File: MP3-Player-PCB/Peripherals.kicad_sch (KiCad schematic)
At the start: 8 parts, among them J401 Micro_SD_Card, Q401 AO3401A, SW401 1-1825910-4, SW402 1-1825910-4, SW403 1-1825910-4, SW404 1-1825910-4

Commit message: Started power schematic
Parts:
- renumbered D401 to D301, D402 to D302, J401 to J301, Q401 to Q301, SW401 to SW301, SW402 to SW302, SW403 to SW303, SW404 to SW304
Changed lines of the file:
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@@
 		(dnp no)
 		(fields_autoplaced yes)
-		(property "Reference" "D402"
+		(property "Reference" "D302"
 			(at 189.23 82.4798 0)
 			(effects
@@
 			(project "MP3-Player"
 				(path "/3f51ea9b-d2e1-4711-a47c-269e1b97e0f4/425fb02a-335c-42f3-aa7e-942bbee7b5dd"
-					(reference "D402")
+					(reference "D302")
 					(unit 1)
 				)
@@
 		(dnp no)
 		(fields_autoplaced yes)
-		(property "Reference" "SW402"
+		(property "Reference" "SW302"
 			(at 93.98 40.64 0)
 			(effects
@@
 			(project "MP3-Player"
 				(path "/3f51ea9b-d2e1-4711-a47c-269e1b97e0f4/425fb02a-335c-42f3-aa7e-942bbee7b5dd"
-					(reference "SW402")
+					(reference "SW302")
 					(unit 1)
 				)
@@
 		(dnp no)
 		(fields_autoplaced yes)
-		(property "Reference" "SW403"
+		(property "Reference" "SW303"
 			(at 72.39 54.61 0)
 			(effects
@@
 			(project "MP3-Player"
 				(path "/3f51ea9b-d2e1-4711-a47c-269e1b97e0f4/425fb02a-335c-42f3-aa7e-942bbee7b5dd"
-					(reference "SW403")
+					(reference "SW303")
 					(unit 1)
 				)
@@
 		(dnp no)
 		(fields_autoplaced yes)
-		(property "Reference" "SW404"
+		(property "Reference" "SW304"
 			(at 93.98 54.61 0)
 			(effects
@@
 			(project "MP3-Player"
 				(path "/3f51ea9b-d2e1-4711-a47c-269e1b97e0f4/425fb02a-335c-42f3-aa7e-942bbee7b5dd"
-					(reference "SW404")
+					(reference "SW304")
 					(unit 1)
 				)
@@
 		(dnp no)
 		(fields_autoplaced yes)
-		(property "Reference" "Q401"
+		(property "Reference" "Q301"
 			(at 121.92 87.6299 0)
 			(effects
@@
 			(project ""
 				(path "/3f51ea9b-d2e1-4711-a47c-269e1b97e0f4/425fb02a-335c-42f3-aa7e-942bbee7b5dd"
-					(reference "Q401")
+					(reference "Q301")
 					(unit 1)
 				)
@@
 		(dnp no)
 		(fields_autoplaced yes)
-		(property "Reference" "D401"
+		(property "Reference" "D301"
 			(at 156.21 82.4798 0)
 			(effects
@@
 			(project "MP3-Player"
 				(path "/3f51ea9b-d2e1-4711-a47c-269e1b97e0f4/425fb02a-335c-42f3-aa7e-942bbee7b5dd"
-					(reference "D401")
+					(reference "D301")
 					(unit 1)
 				)
@@
 		(dnp no)
 		(fields_autoplaced yes)
-		(property "Reference" "SW401"
+		(property "Reference" "SW301"
 			(at 72.39 40.64 0)
 			(effects
@@
 			(project ""
 				(path "/3f51ea9b-d2e1-4711-a47c-269e1b97e0f4/425fb02a-335c-42f3-aa7e-942bbee7b5dd"
-					(reference "SW401")
+					(reference "SW301")
 					(unit 1)
 				)
@@
 		(dnp no)
 		(fields_autoplaced yes)
-		(property "Reference" "J401"
+		(property "Reference" "J301"
 			(at 156.845 34.29 0)
 			(effects
@@
 			(project "MP3-Player"
 				(path "/3f51ea9b-d2e1-4711-a47c-269e1b97e0f4/425fb02a-335c-42f3-aa7e-942bbee7b5dd"
-					(reference "J401")
-					(unit 1)
-				)
+					(reference "J301")
+					(unit 1)
+				)

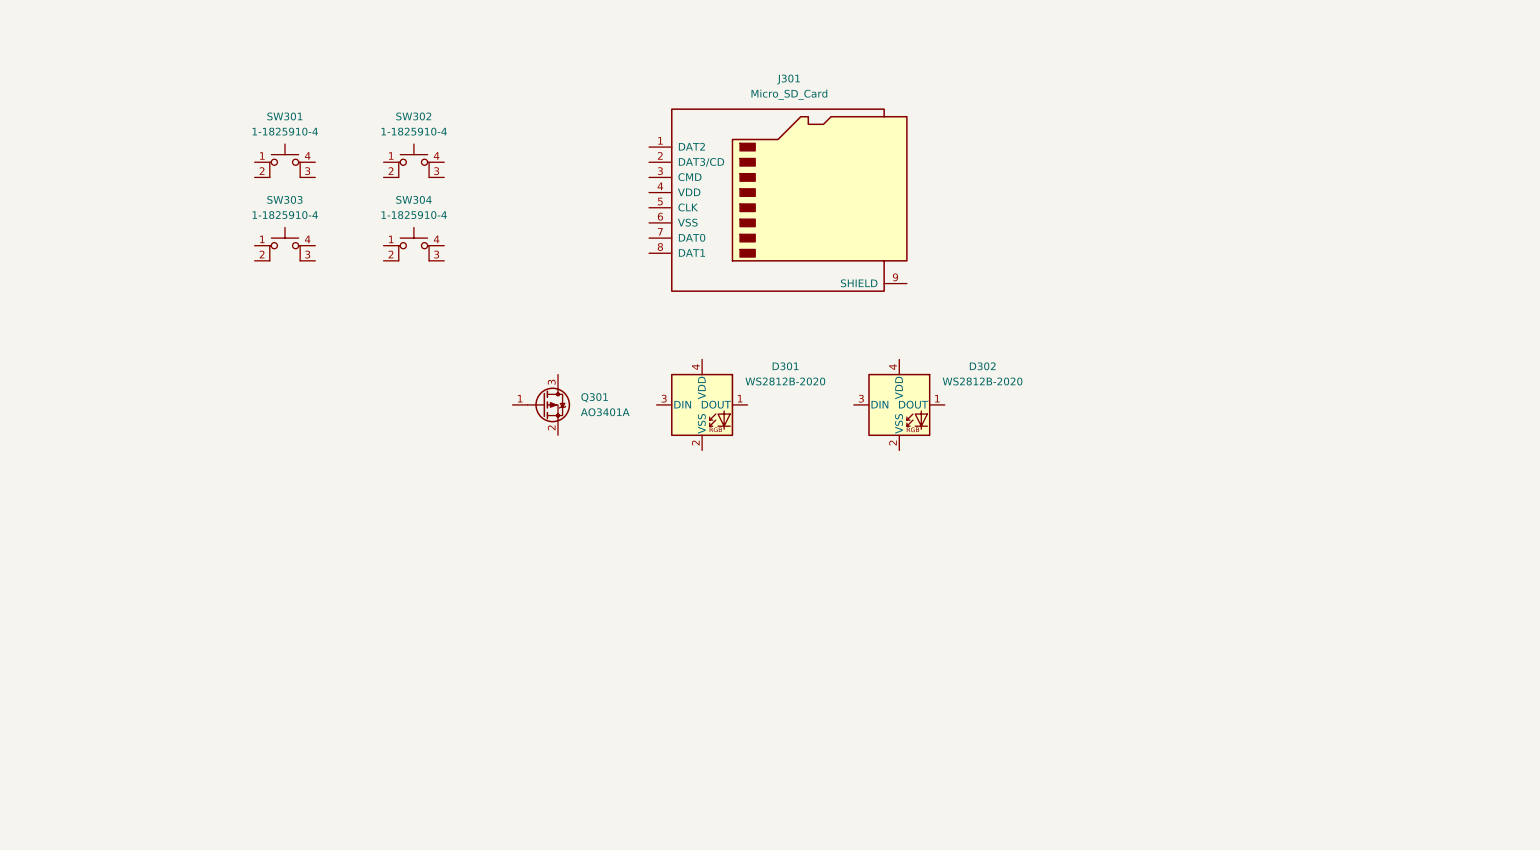
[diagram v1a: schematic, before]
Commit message: Added addressable LED circuitry
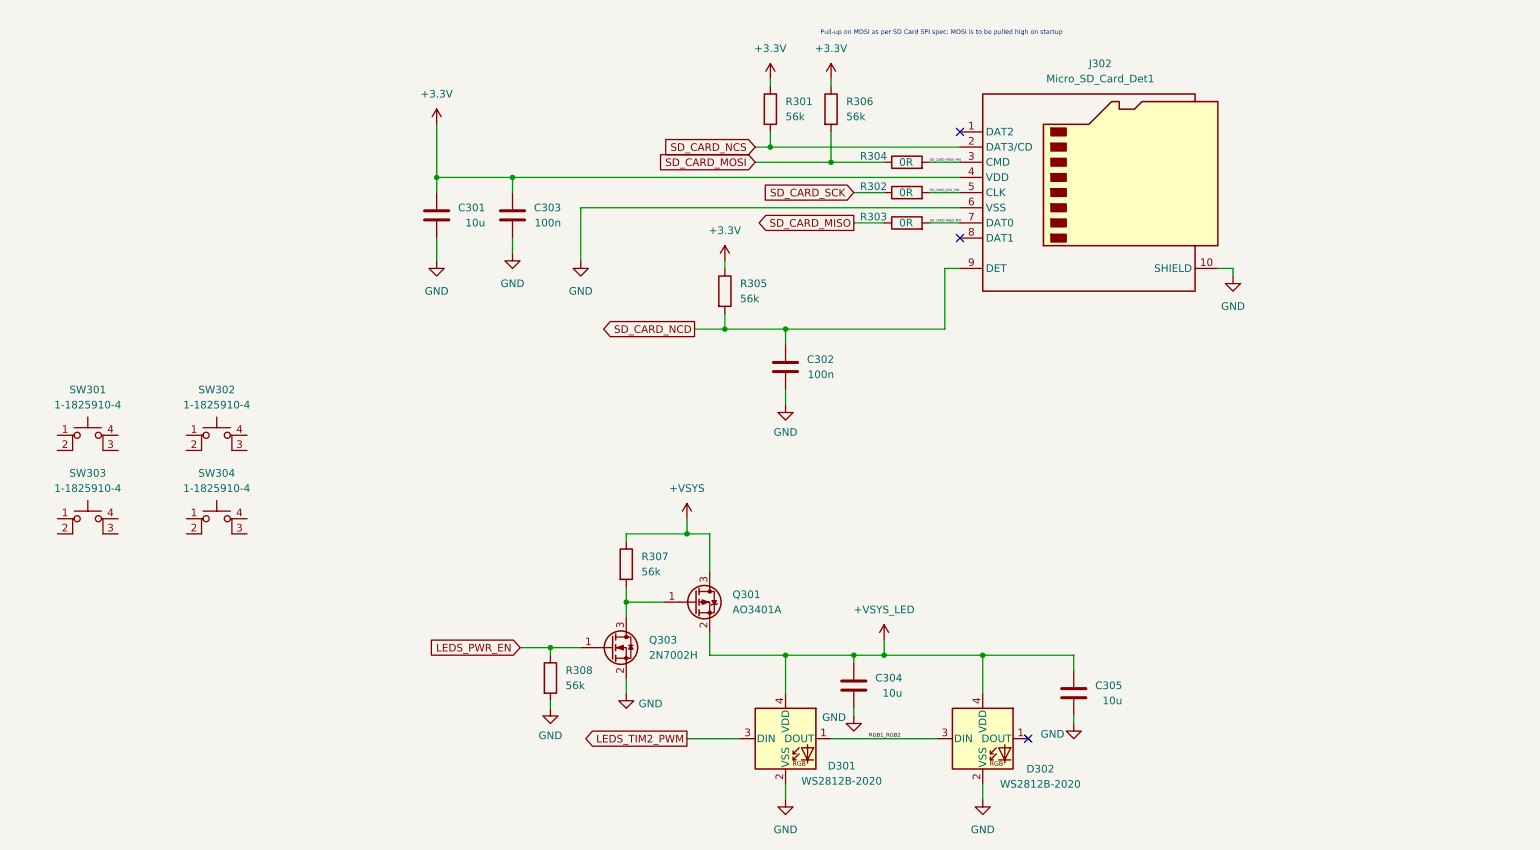
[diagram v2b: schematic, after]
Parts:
- removed J301: Micro_SD_Card, symbol Connector:Micro_SD_Card
- added C301, C304, C305: 10u, symbol Device:C
- added C302, C303: 100n, symbol Device:C
- added J302: Micro_SD_Card_Det1, symbol Connector:Micro_SD_Card_Det1
- added Q303: 2N7002H, Package_TO_SOT_SMD:SOT-23, symbol Transistor_FET:2N7002H
- added R301, R305, R306, R307, R308: 56k, symbol Device:R
- added R302, R303, R304: 0R, symbol Device:R
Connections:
- net GND: now reaches D302.2 (VSS)
- net GND: now also D301.2 (VSS), C301.2, C302.2, C303.2, C304.2, C305.2, J302.10 (SHIELD), J302.6 (VSS), Q303.2 (S), R308.2
- net RGB1_RGB2: now reaches D302.3 (DIN)
- net RGB1_RGB2: now also D301.1 (DOUT)
- net +VSYS_LED: now reaches D302.4 (VDD)
- net +VSYS_LED: now also D301.4 (VDD), Q301.2 (S), C304.1, C305.1
- net at Q301.1 (G): now also Q303.3 (D), R307.2
- net +VSYS: now reaches Q301.3 (D)
- net +VSYS: now also R307.1
- net LEDS_TIM2_PWM: now reaches D301.3 (DIN)
- new net +3.3V: C301.1, C303.1, J302.4 (VDD), R301.1, R305.1, R306.1
- new net LEDS_PWR_EN: Q303.1 (G), R308.1
- new net SD_CARD_MISO: R303.1
- new net SD_CARD_MISO_PIN: J302.7 (DAT0), R303.2
- new net SD_CARD_MOSI: R304.1, R306.2
- new net SD_CARD_MOSI_PIN: J302.3 (CMD), R304.2
- new net SD_CARD_NCD: C302.1, J302.9 (DET), R305.2
- new net SD_CARD_NCS: J302.2 (DAT3/CD), R301.2
- new net SD_CARD_SCK: R302.1
- new net SD_CARD_SCK_PIN: J302.5 (CLK), R302.2
- no-connect marks 0 -> 3
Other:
- note added: "Pull-up on MOSI as per SD Card SPI spec: MOSI is to be pulled high on startup"
- moved on the sheet: D301, D302, Q301, SW301, SW302, SW303, SW304

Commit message: Added button circuitry
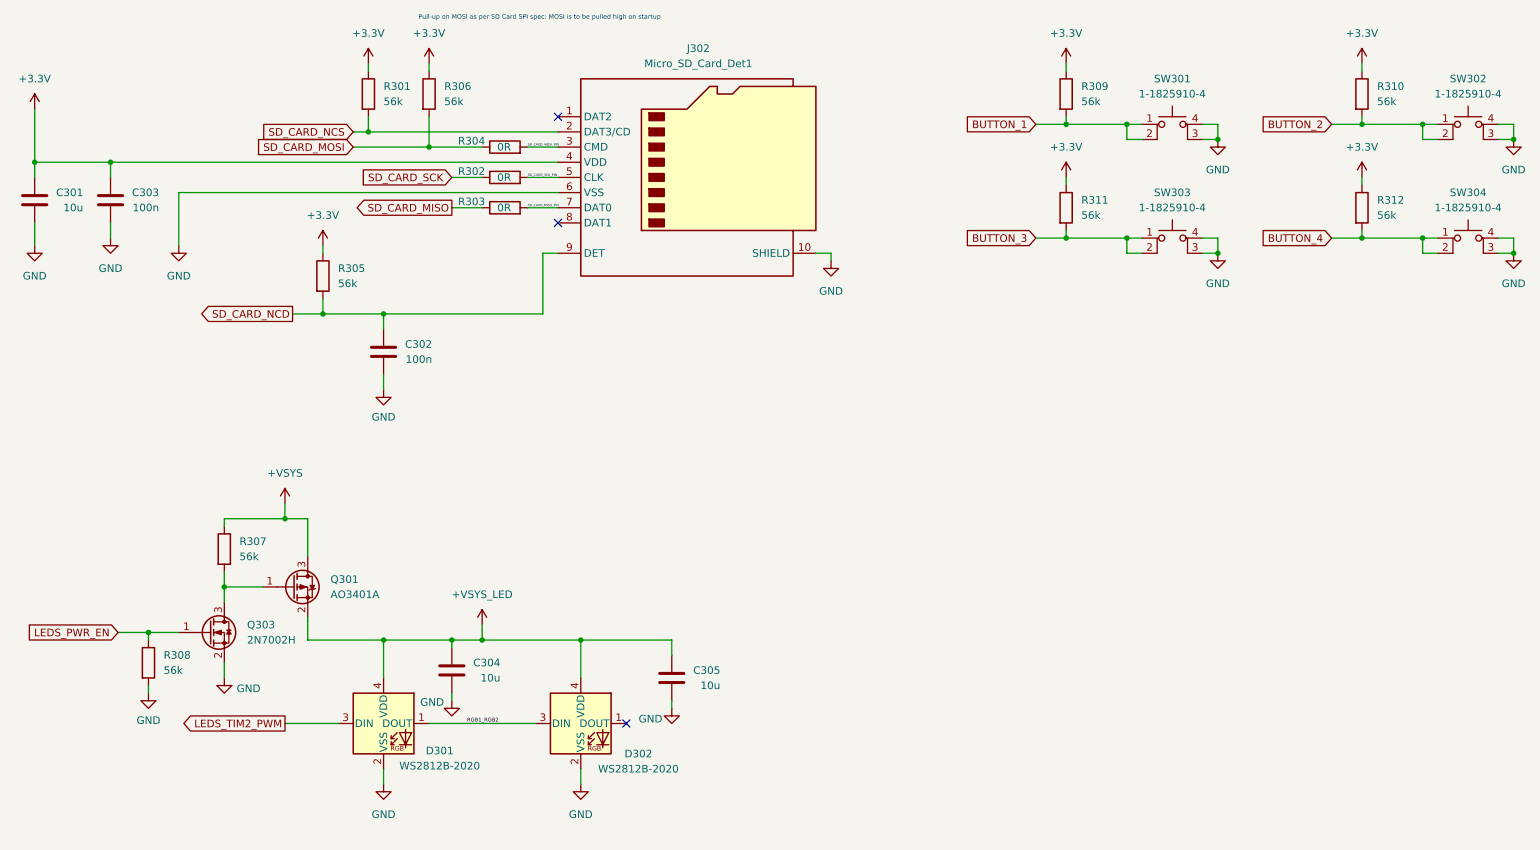
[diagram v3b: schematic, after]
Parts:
- added R309, R310, R311, R312: 56k, symbol Device:R
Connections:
- net +3.3V: now also R309.1, R310.1, R311.1, R312.1
- net GND: now also SW301.3 (K), SW301.4 (A), SW302.3 (K), SW302.4 (A), SW303.3 (K), SW303.4 (A), SW304.3 (K), SW304.4 (A)
- net BUTTON_2: now reaches SW302.1
- net BUTTON_2: now also SW302.2, R310.2
- net BUTTON_3: now reaches SW303.1
- net BUTTON_3: now also SW303.2, R311.2
- net BUTTON_4: now reaches SW304.1
- net BUTTON_4: now also SW304.2, R312.2
- net BUTTON_1: now reaches SW301.1
- net BUTTON_1: now also SW301.2, R309.2
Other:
- moved on the sheet: C301, C302, C303, C304, C305, D301, D302, J302, Q301, Q303, R301, R302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

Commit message: Added esd protection to audiojack and sd card. Also added jack detection on audiojack
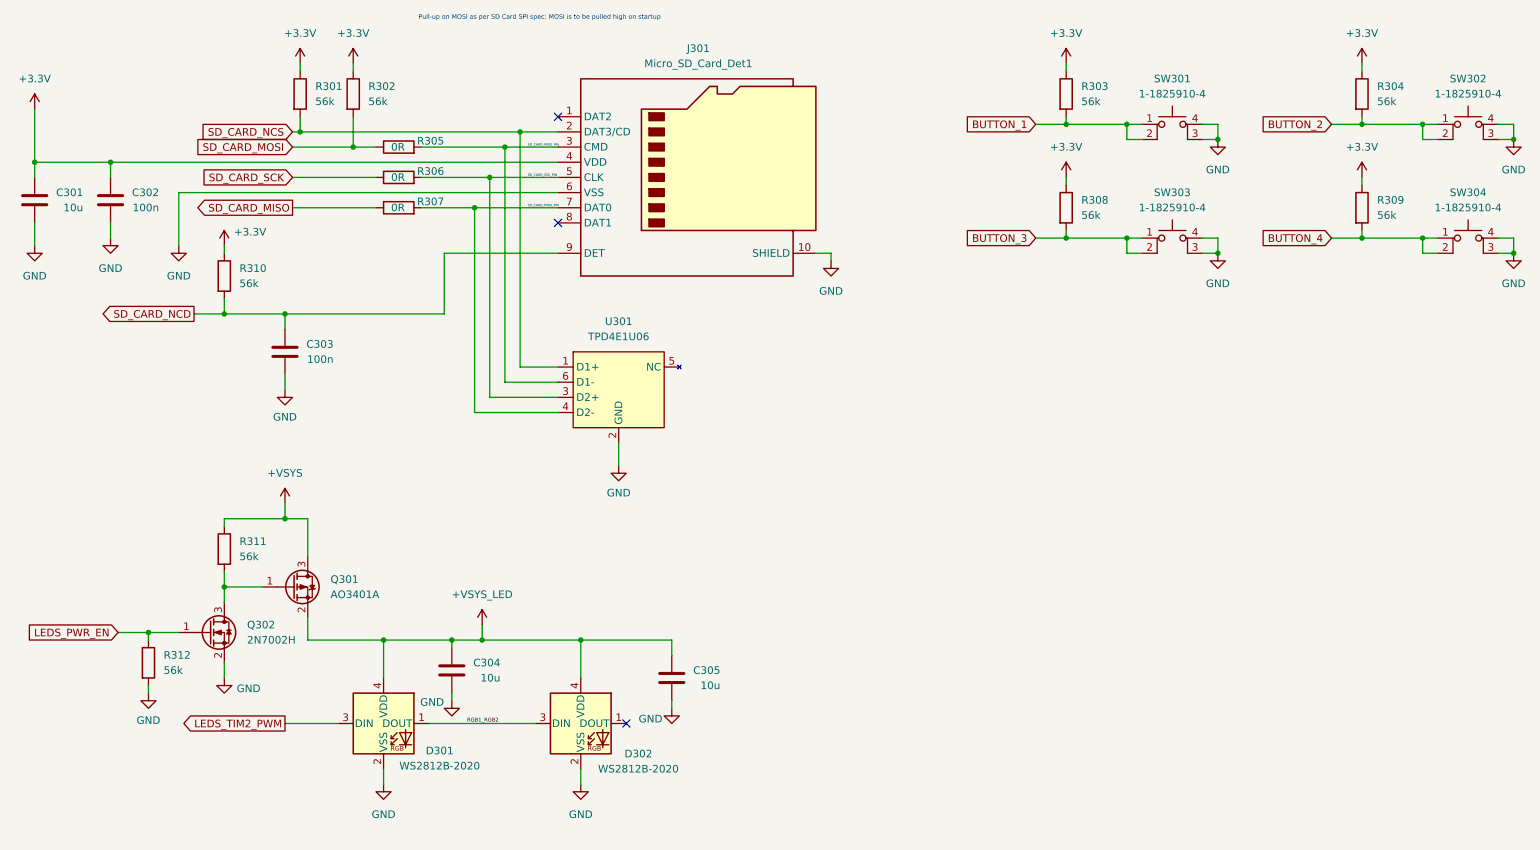
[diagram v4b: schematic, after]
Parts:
- added U301: TPD4E1U06, symbol MP3-Player_Symbol_Libraries:TPD4E1U06
- renumbered C303 to C302, C302 to C303, J302 to J301, Q303 to Q302, R306 to R302, R309 to R303, R310 to R304, R304 to R305, R302 to R306, R303 to R307, R311 to R308, R312 to R309, R305 to R310, R307 to R311, R308 to R312
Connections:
- net GND: now also U301.2 (GND)
- net SD_CARD_MISO_PIN: now also U301.4 (D2-)
- net SD_CARD_MOSI_PIN: now also U301.6 (D1-)
- net SD_CARD_NCS: now also U301.1 (D1+)
- net SD_CARD_SCK_PIN: now also U301.3 (D2+)
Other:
- moved on the sheet: C303, R301, R302, R305, R306, R307, R310

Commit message: Added adc pin and voltage divider to read battery voltage. Also added charging status leds, and assigned some footprints
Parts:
- C301, C304, C305: footprint (none) -> Capacitor_SMD:C_0805_2012Metric
- C302, C303: footprint (none) -> Capacitor_SMD:C_0603_1608Metric
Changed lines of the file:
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@@
 		(on_board yes)
 		(dnp no)
-		(property "Reference" "#PWR0320"
+		(property "Reference" "#PWR0321"
 			(at 62.23 140.97 0)
 			(effects
@@
 			(project "MP3-Player"
 				(path "/3f51ea9b-d2e1-4711-a47c-269e1b97e0f4/425fb02a-335c-42f3-aa7e-942bbee7b5dd"
-					(reference "#PWR0320")
+					(reference "#PWR0321")
 					(unit 1)
 				)
@@
 		(on_board yes)
 		(dnp no)
-		(property "Reference" "#PWR0321"
+		(property "Reference" "#PWR0322"
 			(at 49.53 143.51 0)
 			(effects
@@
 			(project "MP3-Player"
 				(path "/3f51ea9b-d2e1-4711-a47c-269e1b97e0f4/425fb02a-335c-42f3-aa7e-942bbee7b5dd"
-					(reference "#PWR0321")
+					(reference "#PWR0322")
 					(unit 1)
 				)
@@
 			)
 		)
-		(property "Footprint" ""
+		(property "Footprint" "Capacitor_SMD:C_0603_1608Metric"
 			(at 42.2148 58.42 0)
 			(effects
@@
 		(dnp no)
 		(fields_autoplaced yes)
-		(property "Reference" "#PWR0325"
+		(property "Reference" "#PWR0326"
 			(at 121.92 158.75 0)
 			(effects
@@
 			(project "MP3-Player"
 				(path "/3f51ea9b-d2e1-4711-a47c-269e1b97e0f4/425fb02a-335c-42f3-aa7e-942bbee7b5dd"
-					(reference "#PWR0325")
+					(reference "#PWR0326")
 					(unit 1)
 				)
@@
 		(on_board yes)
 		(dnp no)
-		(property "Reference" "#PWR0323"
+		(property "Reference" "#PWR0324"
 			(at 137.16 146.05 0)
 			(effects
@@
 			(project "MP3-Player"
 				(path "/3f51ea9b-d2e1-4711-a47c-269e1b97e0f4/425fb02a-335c-42f3-aa7e-942bbee7b5dd"
-					(reference "#PWR0323")
+					(reference "#PWR0324")
 					(unit 1)
 				)
@@
 			)
 		)
-		(property "Footprint" ""
+		(property "Footprint" "Capacitor_SMD:C_0603_1608Metric"
 			(at 71.4248 83.82 0)
 			(effects
@@
 			)
 		)
-		(property "Footprint" ""
+		(property "Footprint" "Capacitor_SMD:C_0805_2012Metric"
 			(at 29.5148 58.42 0)
 			(effects
@@
 		(dnp no)
 		(fields_autoplaced yes)
-		(property "Reference" "#PWR0319"
+		(property "Reference" "#PWR0320"
 			(at 105.41 129.54 0)
 			(effects
@@
 			(project "MP3-Player"
 				(path "/3f51ea9b-d2e1-4711-a47c-269e1b97e0f4/425fb02a-335c-42f3-aa7e-942bbee7b5dd"
-					(reference "#PWR0319")
+					(reference "#PWR0320")
 					(unit 1)
 				)
@@
 		(dnp no)
 		(fields_autoplaced yes)
-		(property "Reference" "#PWR0318"
+		(property "Reference" "#PWR0319"
 			(at 72.39 109.22 0)
 			(effects
@@
 			(project "MP3-Player"
 				(path "/3f51ea9b-d2e1-4711-a47c-269e1b97e0f4/425fb02a-335c-42f3-aa7e-942bbee7b5dd"
-					(reference "#PWR0318")
+					(reference "#PWR0319")
 					(unit 1)
 				)
@@
 			)
 		)
-		(property "Footprint" ""
+		(property "Footprint" "Capacitor_SMD:C_0805_2012Metric"
 			(at 99.3648 137.16 0)
 			(effects
@@
 		(on_board yes)
 		(dnp no)
-		(property "Reference" "#PWR0322"
+		(property "Reference" "#PWR0323"
 			(at 100.33 144.78 0)
 			(effects
@@
 			(project "MP3-Player"
 				(path "/3f51ea9b-d2e1-4711-a47c-269e1b97e0f4/425fb02a-335c-42f3-aa7e-942bbee7b5dd"
-					(reference "#PWR0322")
+					(reference "#PWR0323")
 					(unit 1)
 				)
@@
 		(on_board yes)
 		(dnp no)
-		(property "Reference" "#PWR0326"
+		(property "Reference" "#PWR0318"
 			(at 128.27 105.41 0)
 			(effects
@@
 			(project "MP3-Player"
 				(path "/3f51ea9b-d2e1-4711-a47c-269e1b97e0f4/425fb02a-335c-42f3-aa7e-942bbee7b5dd"
-					(reference "#PWR0326")
+					(reference "#PWR0318")
 					(unit 1)
 				)
@@
 			)
 		)
-		(property "Footprint" ""
+		(property "Footprint" "Capacitor_SMD:C_0805_2012Metric"
 			(at 136.1948 138.43 0)
 			(effects
@@
 		(dnp no)
 		(fields_autoplaced yes)
-		(property "Reference" "#PWR0324"
+		(property "Reference" "#PWR0325"
 			(at 88.9 158.75 0)
 			(effects
@@
 			(project "MP3-Player"
 				(path "/3f51ea9b-d2e1-4711-a47c-269e1b97e0f4/425fb02a-335c-42f3-aa7e-942bbee7b5dd"
-					(reference "#PWR0324")
+					(reference "#PWR0325")
 					(unit 1)
 				)
